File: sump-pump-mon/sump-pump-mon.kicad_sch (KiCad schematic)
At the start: 38 parts, among them J1 Main Input, J2 Wall Power, J3 Battery, J4 Conn_01x06_Pin, J5 Aux Input, SW1 SW_Push, SW2 SW_Push, SW3 MODE, SW4 POWER, U1 L7805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

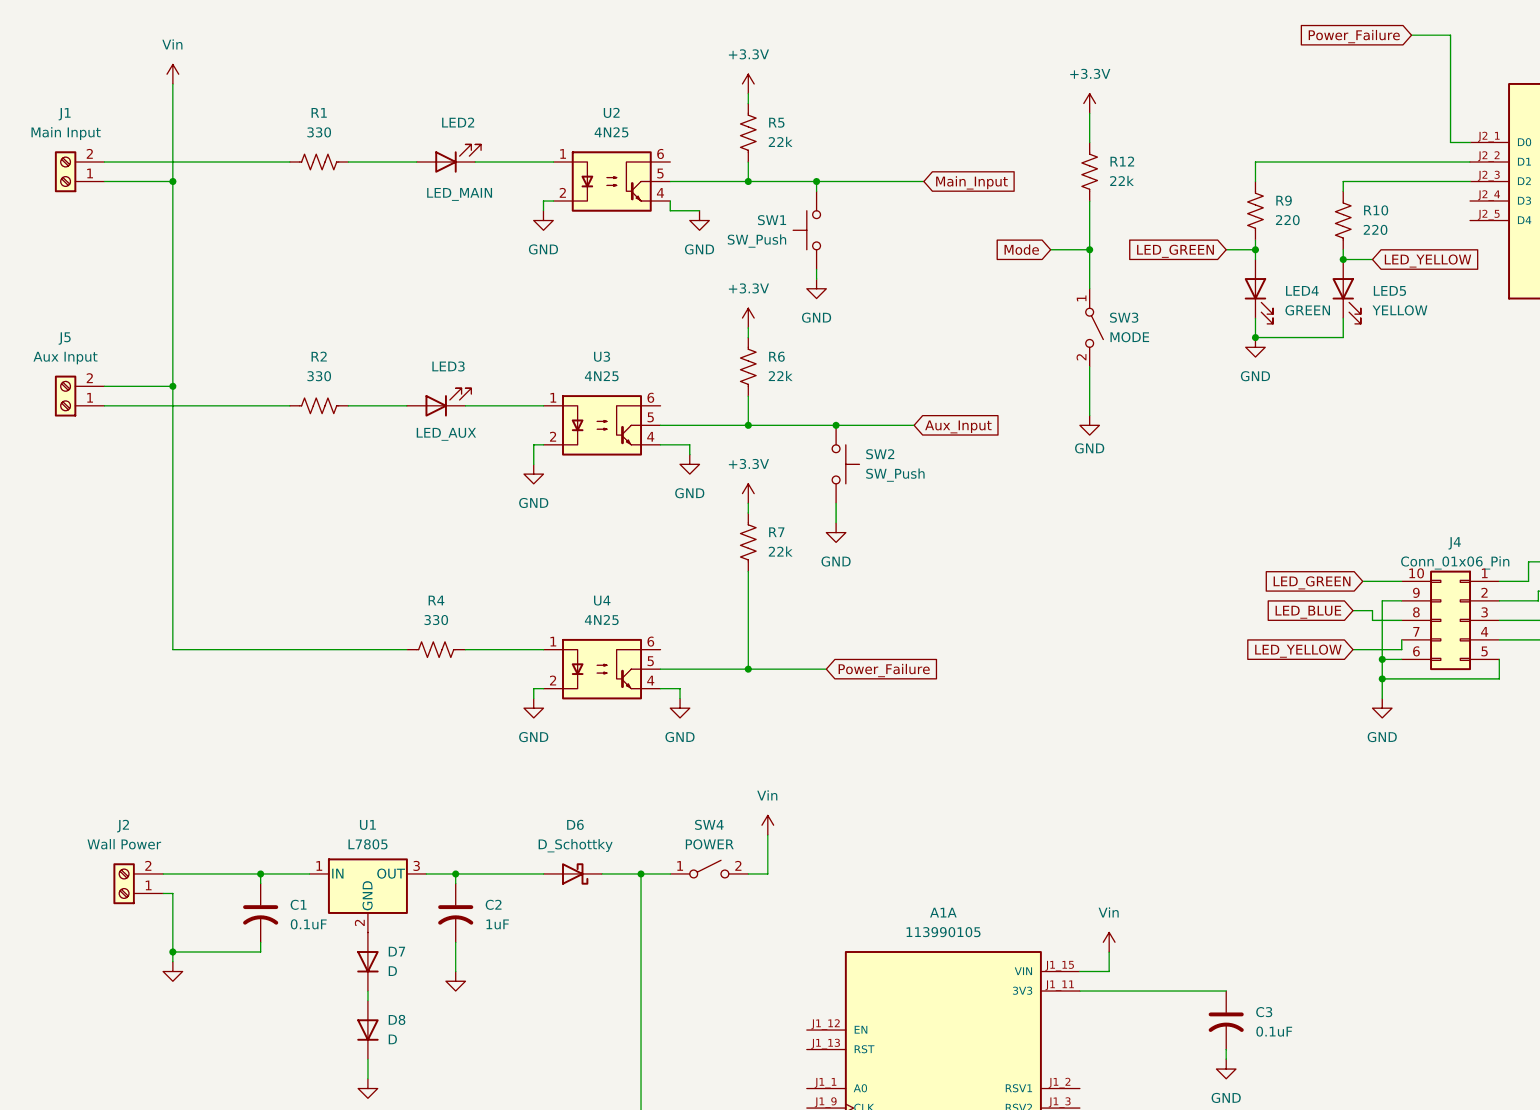
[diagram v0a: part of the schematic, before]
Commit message: Rough parts placement and partial routing
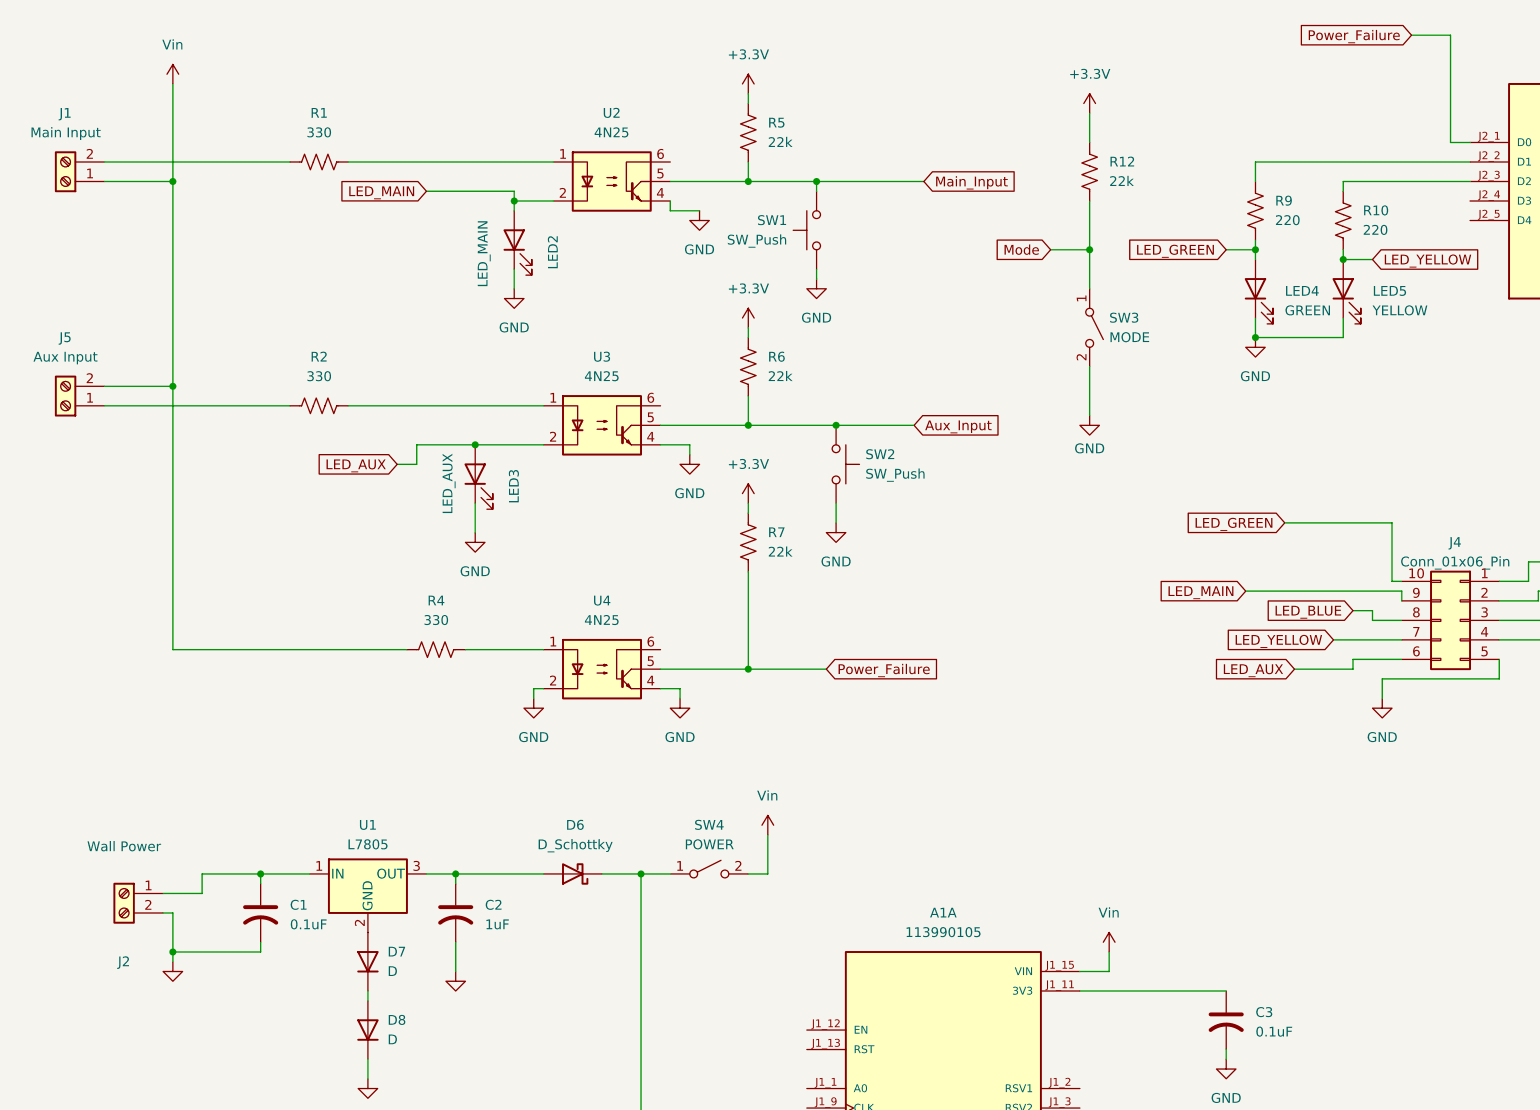
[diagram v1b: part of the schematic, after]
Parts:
- J4: footprint Connector_JST:JST_XH_B6B-XH-A_1x06_P2.50mm_Vertical -> Connector_JST:JST_XH_B10B-XH-A_1x10_P2.50mm_Vertical
- LED1, LED2, LED3, LED4, LED5, LED6: footprint LED_THT:LED_D5.0mm -> (none)
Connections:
- net GND: now also J2.2 (Pin_2), LED2.1 (K), LED3.1 (K); no longer J2.1 (Pin_1), J4.6 (Pin_6), J4.9 (Pin_9), U2.2, U3.2
- net at C1.1, U1.1 (IN): now also J2.1 (Pin_1); no longer J2.2 (Pin_2)
- net at R1.2: now also U2.1; no longer LED2.2 (A)
- net at R2.2: now also U3.1; no longer LED3.2 (A)
- new net LED_AUX: J4.6 (Pin_6), LED3.2 (A), U3.2
- new net LED_MAIN: J4.9 (Pin_9), LED2.2 (A), U2.2
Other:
- moved on the sheet: J2, LED2, LED3

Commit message: Routing complete
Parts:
- added H1, H2, H3, H4: MountingHole, MountingHole:MountingHole_3.7mm, symbol Mechanical:MountingHole
- added HS1: Heatsink, symbol Mechanical:Heatsink
- added J6: I2C, Connector_JST:JST_XH_B2B-XH-A_1x02_P2.50mm_Vertical, symbol Connector:Conn_01x02_Pin
- added R13, R14: 2.7k, Resistor_THT:R_Axial_DIN0207_L6.3mm_D2.5mm_P10.16mm_Horizontal, symbol Device:R_US
- J2, J3: footprint TerminalBlock_Phoenix:TerminalBlock_Phoenix_MKDS-1,5-2-5.08_1x02_P5.08mm_Horizontal -> Connector_JST:JST_XH_B2B-XH-A_1x02_P2.50mm_Vertical; symbol Connector:Screw_Terminal_01x02 -> Connector:Conn_01x02_Pin
- J4: value Conn_01x06_Pin -> Display_Conn; footprint Connector_JST:JST_XH_B10B-XH-A_1x10_P2.50mm_Vertical -> Connector_JST:JST_XH_B12B-XH-A_1x12_P2.50mm_Vertical; symbol Connector_Generic:Conn_02x05_Counter_Clockwise -> Connector:Conn_01x12_Pin
- U1: footprint Package_TO_SOT_THT:TO-220-3_Horizontal_TabDown -> Package_TO_SOT_THT:TO-220-3_Vertical
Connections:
- net +3.3V: now also A1.J1_11 (3V3), C3.1, J4.11 (Pin_11), LED4.2 (A), LED5.2 (A), R13.1, R14.1
- net GND: now also J4.12 (Pin_12); no longer LED4.1 (K), LED5.1 (K)
- net LED_GREEN: now also LED4.1 (K); no longer LED4.2 (A)
- net LED_YELLOW: now also LED5.1 (K); no longer LED5.2 (A)
- net at A1.J2_3 (D2): now also J6.2 (Pin_2), R14.2; no longer R10.1
- net at A1.J2_2 (D1): now also J6.1 (Pin_1), R13.2; no longer R9.1
- net at A1.J2_4 (D3): now also R9.1
- net at A1.J2_5 (D4): now also R10.1
- net LED_POWER renamed LED_6V
- no-connect marks 0 -> 16
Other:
- moved on the sheet: LED4, LED5, R10, R9

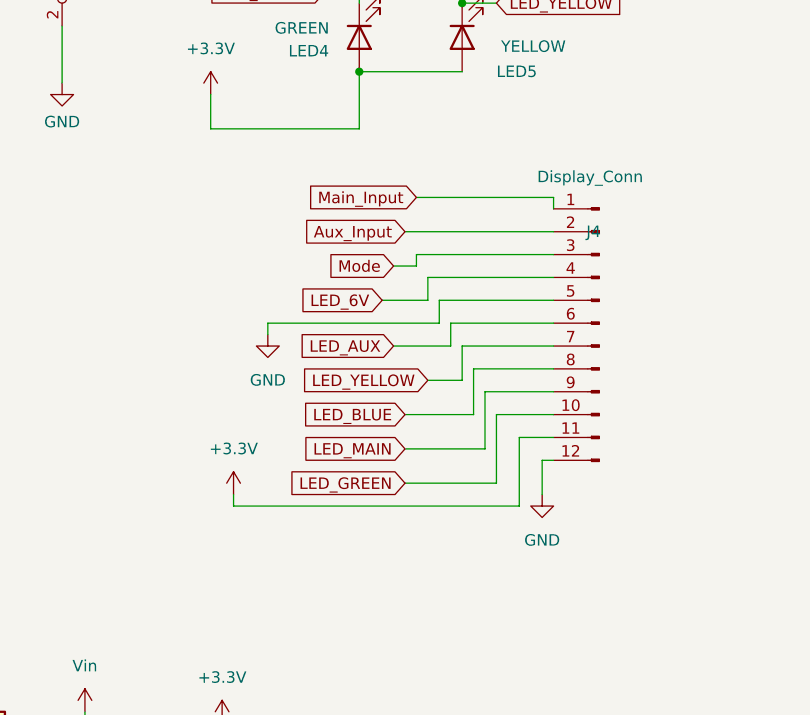
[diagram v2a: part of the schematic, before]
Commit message: Redid layout to shrink size and add ground plane
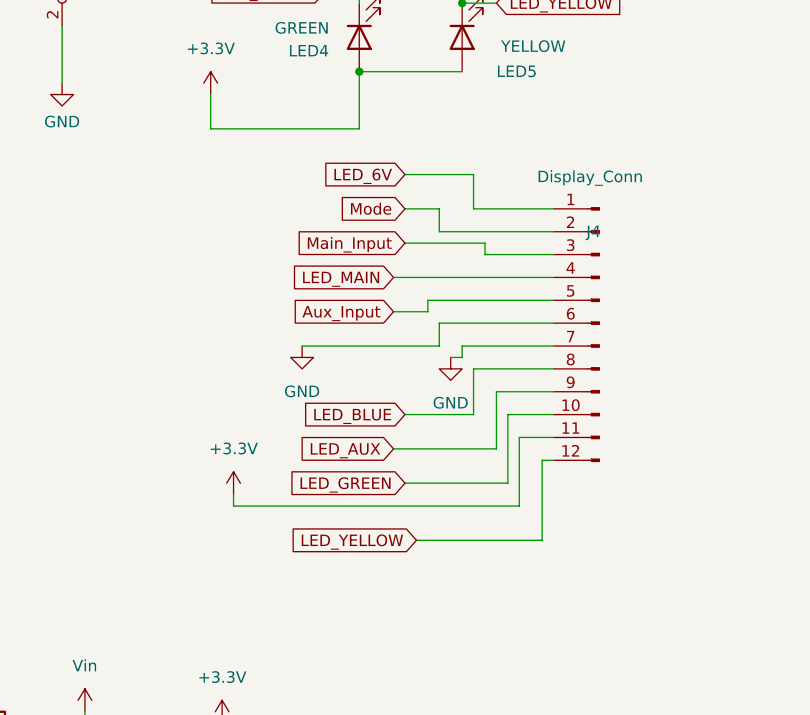
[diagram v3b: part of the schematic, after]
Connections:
- net Aux_Input: now also J4.5 (Pin_5); no longer J4.2 (Pin_2)
- net GND: now also J4.6 (Pin_6), J4.7 (Pin_7); no longer J4.12 (Pin_12), J4.5 (Pin_5)
- net LED_6V: now also J4.1 (Pin_1); no longer J4.4 (Pin_4)
- net LED_AUX: now also J4.9 (Pin_9); no longer J4.6 (Pin_6)
- net LED_MAIN: now also J4.4 (Pin_4); no longer J4.9 (Pin_9)
- net LED_YELLOW: now also J4.12 (Pin_12); no longer J4.7 (Pin_7)
- net Main_Input: now also J4.3 (Pin_3); no longer J4.1 (Pin_1)
- net Mode: now also J4.2 (Pin_2); no longer J4.3 (Pin_3)

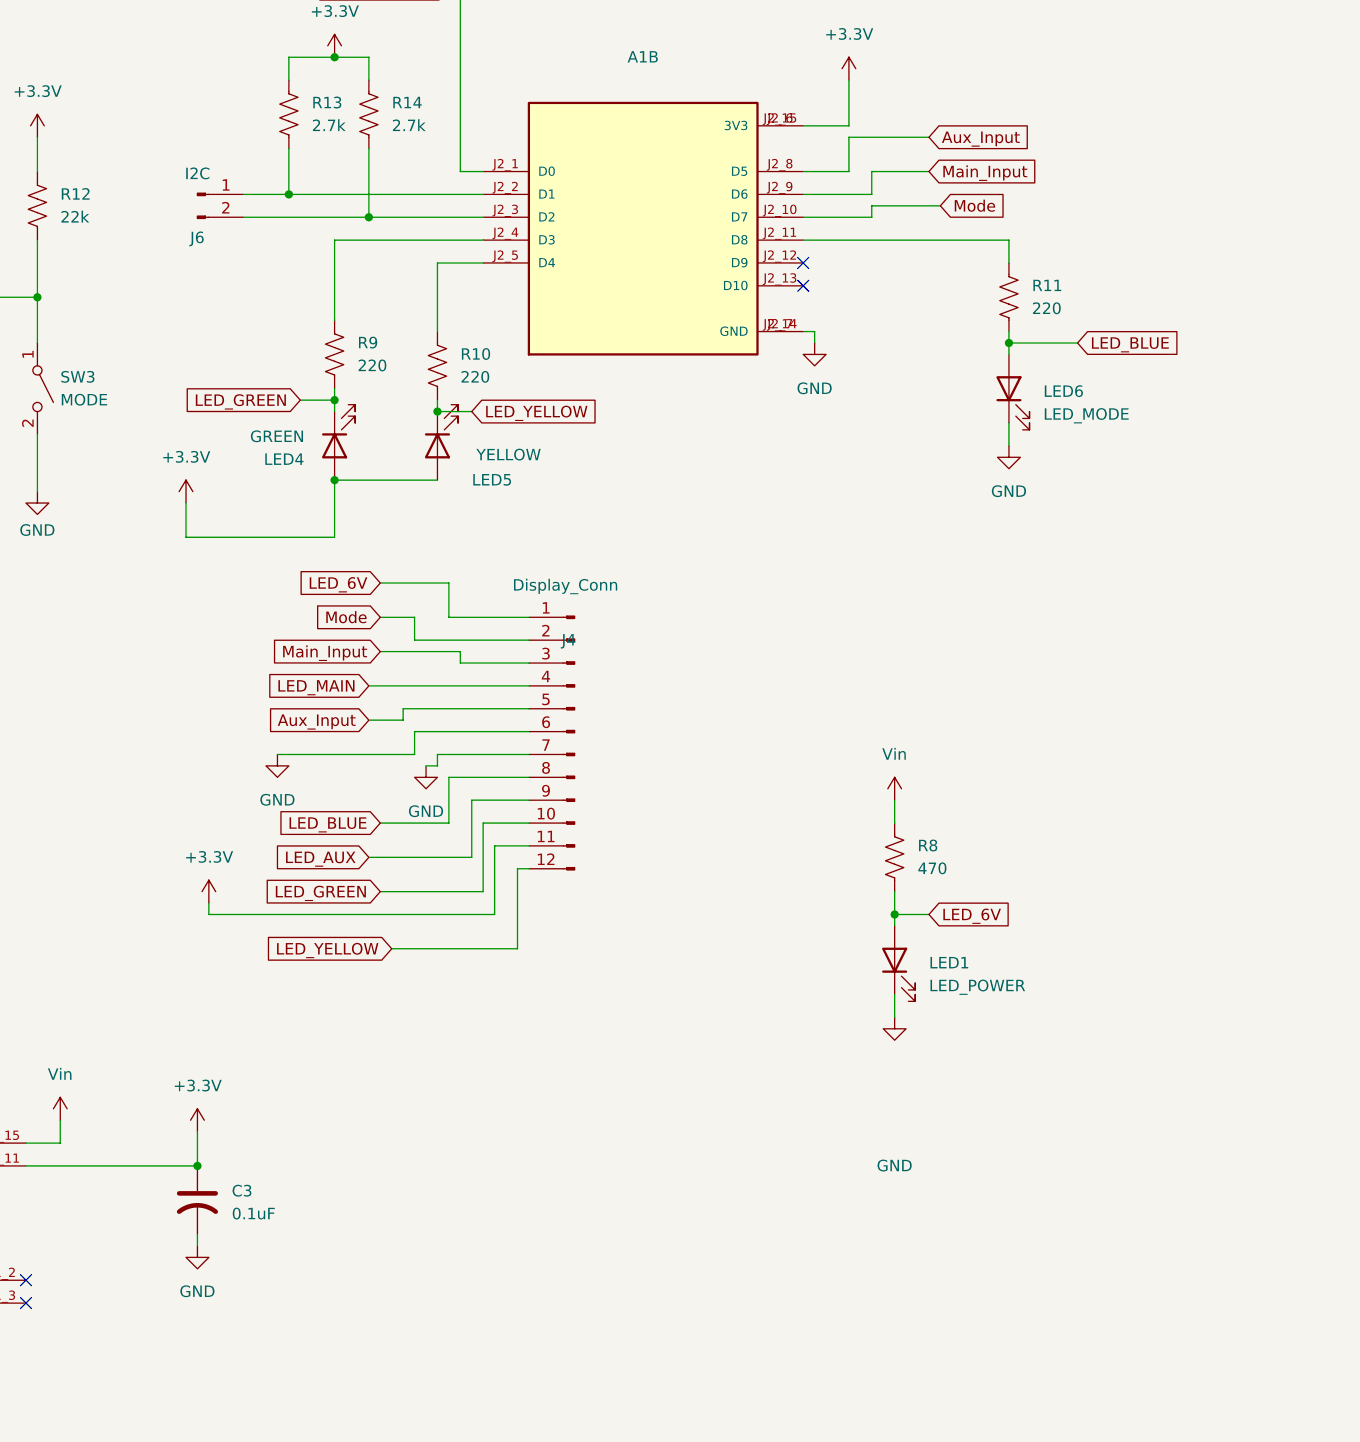
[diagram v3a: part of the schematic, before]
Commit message: Add GND to I2C connector
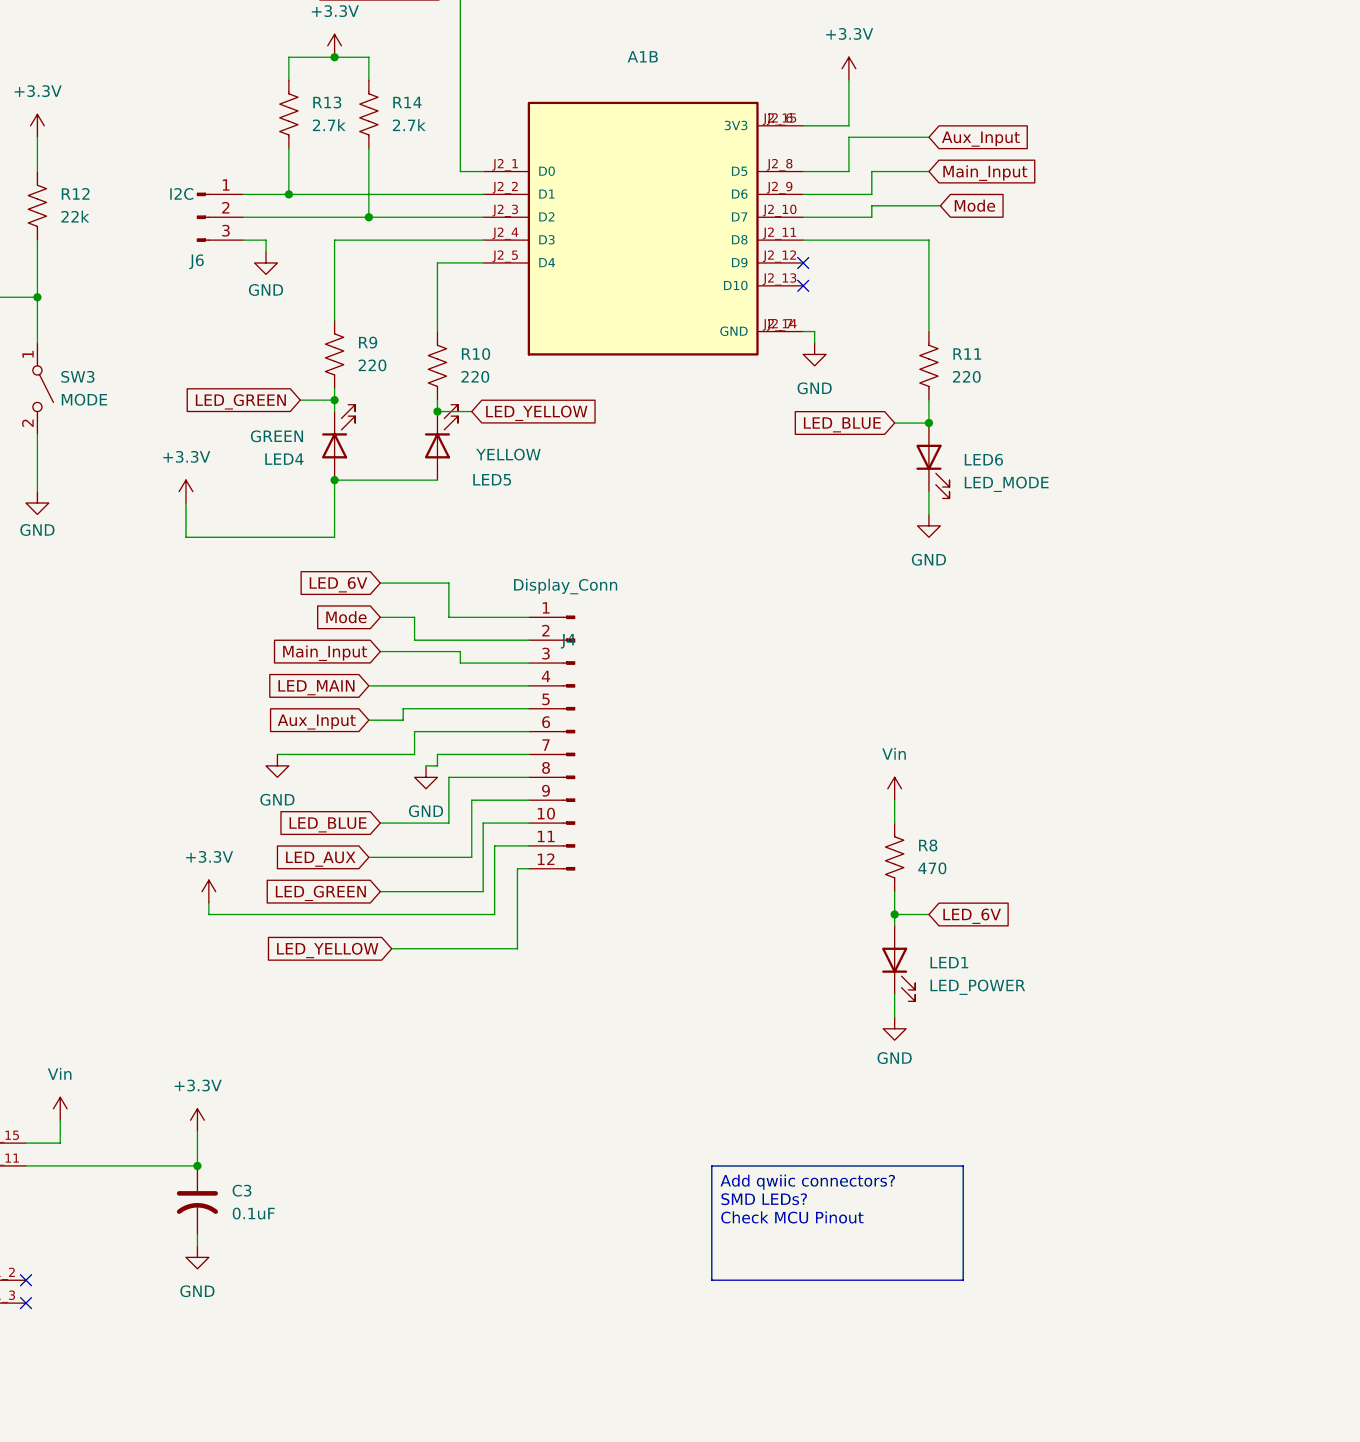
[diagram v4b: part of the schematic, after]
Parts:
- J6: footprint Connector_JST:JST_XH_B2B-XH-A_1x02_P2.50mm_Vertical -> Connector_JST:JST_XH_B3B-XH-A_1x03_P2.50mm_Vertical; symbol Connector:Conn_01x02_Pin -> Connector:Conn_01x03_Pin
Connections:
- net GND: now also J6.3 (Pin_3)
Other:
- title: (none) -> Sump Pump Monitor
- moved on the sheet: LED6, R11
